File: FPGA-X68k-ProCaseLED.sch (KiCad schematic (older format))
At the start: 47 parts, among them J1 Conn_01x05_Male, SW1 SW_DIP_x04, U1 TLC59116IPWR

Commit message: First version
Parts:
- added TP25: RESET, TestPoint:TestPoint_THTPad_D1.5mm_Drill0.7mm, symbol Connector:TestPoint
- added TP26: SCL, TestPoint:TestPoint_THTPad_D1.5mm_Drill0.7mm, symbol Connector:TestPoint
- added TP27: SDA, TestPoint:TestPoint_THTPad_D1.5mm_Drill0.7mm, symbol Connector:TestPoint
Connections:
- net RESET: now also TP25.1
- net SCL: now also TP26.1
- net SDA: now also TP27.1
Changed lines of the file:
@@
 Connection ~ 2950 3850
 Wire Wire Line
-	1250 3850 2950 3850
+	1250 3850 2750 3850
 Connection ~ 2650 3750
 Wire Wire Line
 	2650 3750 3350 3750
 Wire Wire Line
-	1250 3750 2650 3750
+	1250 3750 2450 3750
 $Comp
 L power:+3.3V #PWR06
@@
 Connection ~ 2350 3650
 Wire Wire Line
-	2350 3650 1250 3650
+	2350 3650 2150 3650
 Text Label 1600 3650 0    50   ~ 0
 RESET
@@
 Wire Wire Line
 	4400 1700 4200 1700
+Connection ~ 4200 1700
+Wire Wire Line
+	4200 1700 4200 2050
+$Comp
+L Connector:TestPoint TP25
+U 1 1 5F30828E
+P 2150 3600
+F 0 "TP25" H 2208 3718 50  0000 L CNN
+F 1 "RESET" H 2208 3627 50  0000 L CNN
+F 2 "TestPoint:TestPoint_THTPad_D1.5mm_Drill0.7mm" H 2350 3600 50  0001 C CNN
+F 3 "~" H 2350 3600 50  0001 C CNN
+	1    2150 3600
+	1    0    0    -1
+$EndComp
+$Comp
+L Connector:TestPoint TP26
+U 1 1 5F308F76
+P 2450 3600
+F 0 "TP26" H 2508 3718 50  0000 L CNN
+F 1 "SCL" H 2508 3627 50  0000 L CNN
+F 2 "TestPoint:TestPoint_THTPad_D1.5mm_Drill0.7mm" H 2650 3600 50  0001 C CNN
+F 3 "~" H 2650 3600 50  0001 C CNN
+	1    2450 3600
+	1    0    0    -1
+$EndComp
+$Comp
+L Connector:TestPoint TP27
+U 1 1 5F3091EF
+P 2750 3600
+F 0 "TP27" H 2808 3718 50  0000 L CNN
+F 1 "SDA" H 2808 3627 50  0000 L CNN
+F 2 "TestPoint:TestPoint_THTPad_D1.5mm_Drill0.7mm" H 2950 3600 50  0001 C CNN
+F 3 "~" H 2950 3600 50  0001 C CNN
+	1    2750 3600
+	1    0    0    -1
+$EndComp
+Wire Wire Line
+	2150 3600 2150 3650
+Connection ~ 2150 3650
+Wire Wire Line
+	2150 3650 1250 3650
+Wire Wire Line
+	2450 3600 2450 3750
+Connection ~ 2450 3750
+Wire Wire Line
+	2450 3750 2650 3750
+Wire Wire Line
+	2750 3600 2750 3850
 Wire Bus Line
 	8150 700  8150 6400
@@
 Wire Bus Line
 	5350 2300 5350 6400
-Connection ~ 4200 1700
-Wire Wire Line
-	4200 1700 4200 2050
+Connection ~ 2750 3850
+Wire Wire Line
+	2750 3850 2950 3850
 $EndSCHEMATC

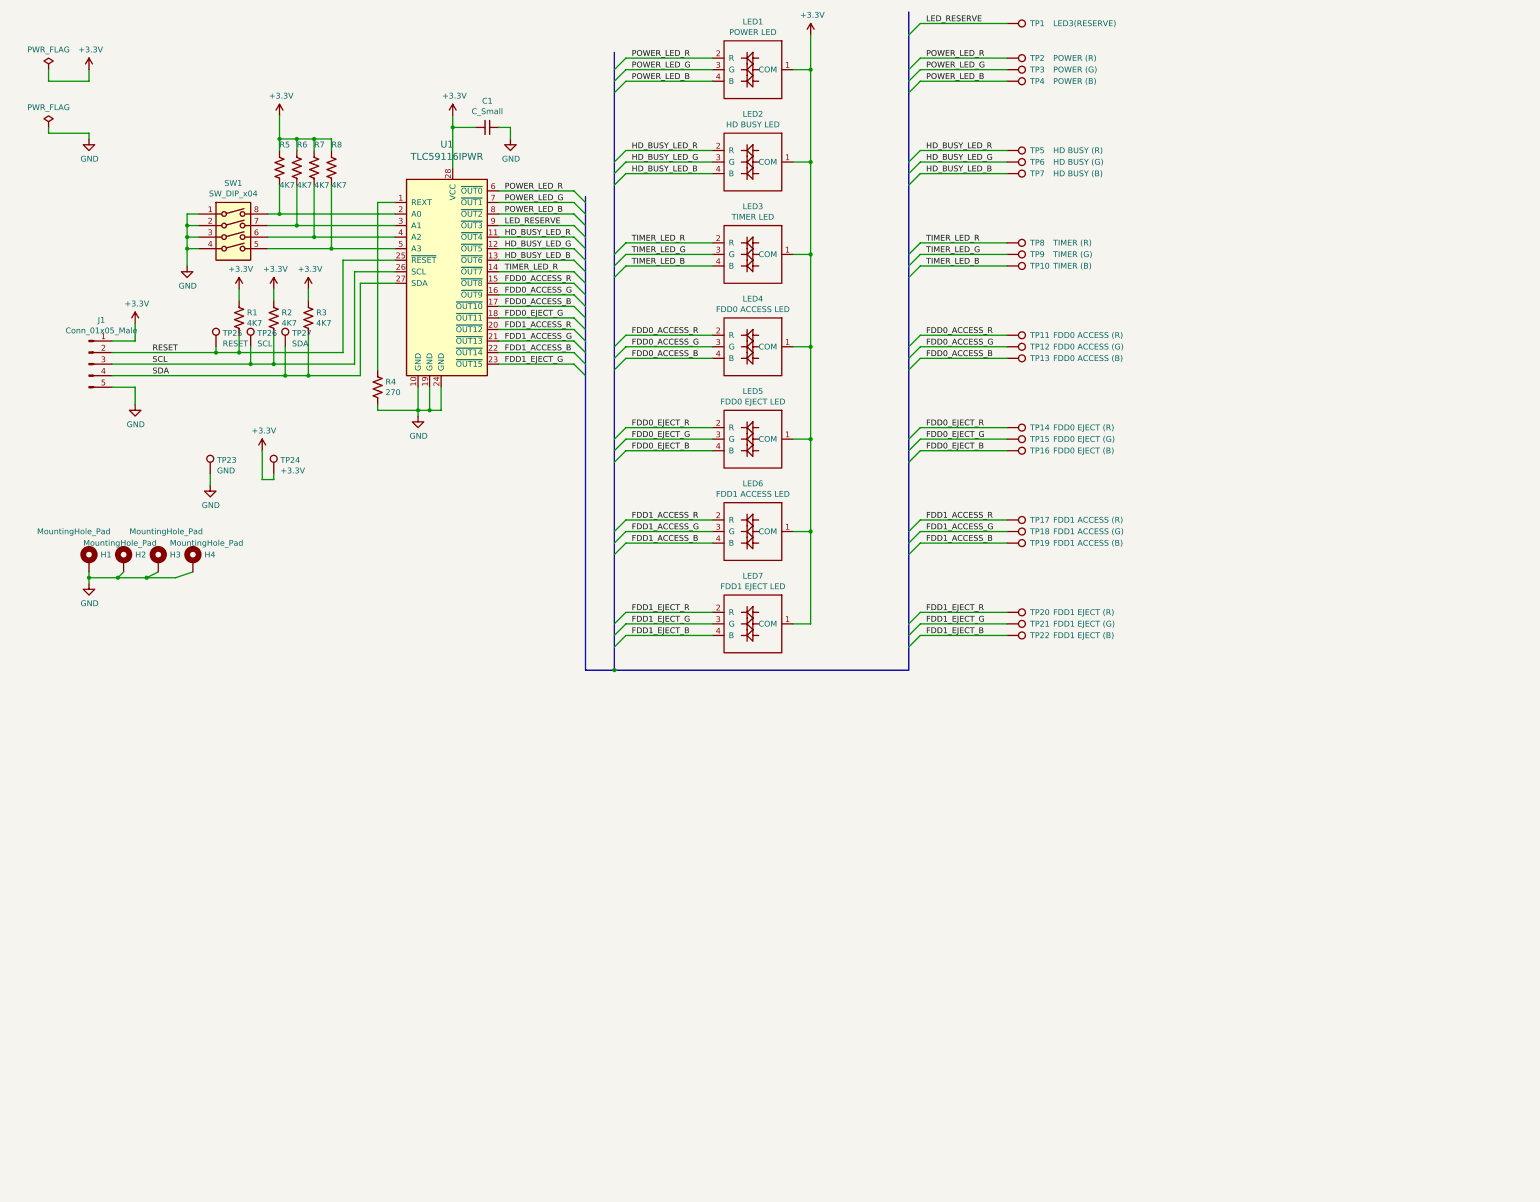
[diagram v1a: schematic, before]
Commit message: Add miniature FDD sensor circuit.
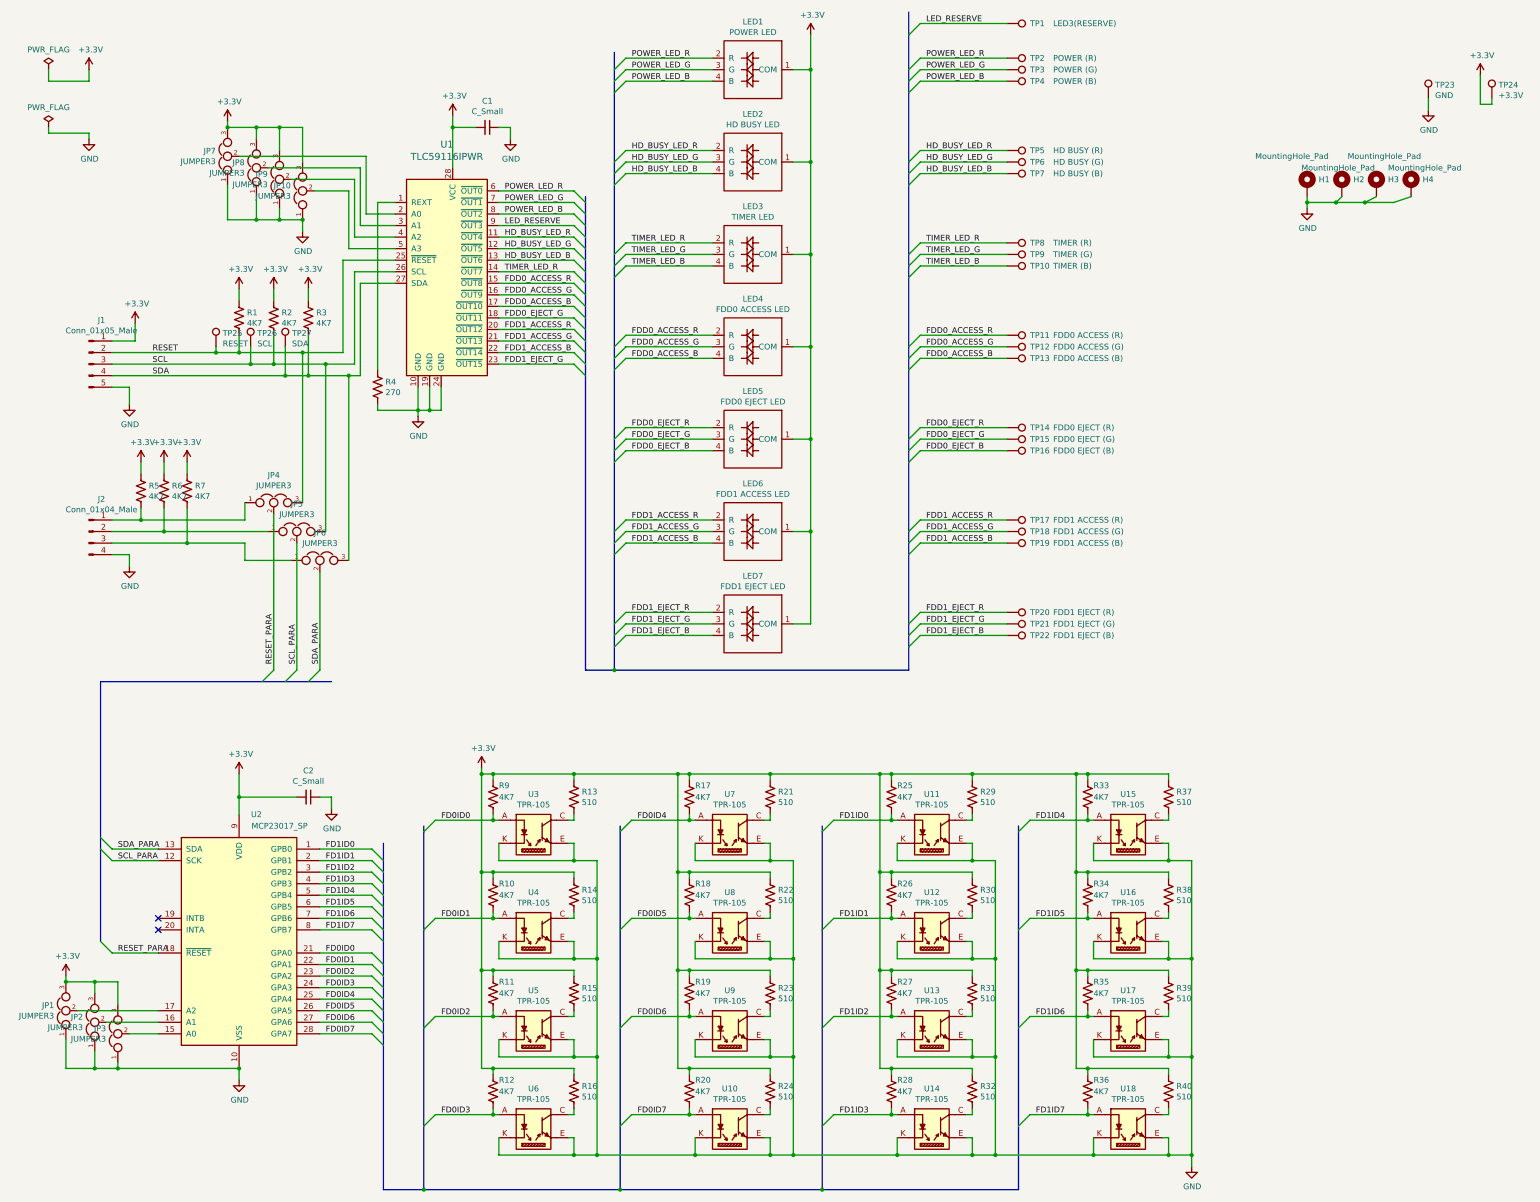
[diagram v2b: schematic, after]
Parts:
- removed R8: 4K7, Resistor_SMD:R_0603_1608Metric_Pad1.05x0.95mm_HandSolder, symbol Device:R_US
- removed SW1: SW_DIP_x04, Button_Switch_SMD:SW_DIP_SPSTx04_Slide_Copal_CHS-04B_W7.62mm_P1.27mm, symbol Switch:SW_DIP_x04
- added C2: C_Small, Capacitor_SMD:C_0603_1608Metric_Pad1.05x0.95mm_HandSolder, symbol Device:C_Small
- added J2: Conn_01x04_Male, Connector_JST:JST_EH_S4B-EH_1x04_P2.50mm_Horizontal, symbol Connector:Conn_01x04_Male
- added JP1, JP10, JP2, JP3, JP4, JP5, JP6, JP7, JP8, JP9: JUMPER3, Jumper:SolderJumper-3_P1.3mm_Open_RoundedPad1.0x1.5mm_NumberLabels, symbol device:JUMPER3
- added R10, R11, R12, R17, R18, R19, R20, R25, R26, R27, R28, R33, R34, R35, R36, R9: 4K7, Resistor_SMD:R_0603_1608Metric_Pad1.05x0.95mm_HandSolder, symbol Device:R_US
- added R13, R14, R15, R16, R21, R22, R23, R24, R29, R30, R31, R32, R37, R38, R39, R40: 510, Resistor_SMD:R_0603_1608Metric_Pad1.05x0.95mm_HandSolder, symbol Device:R_US
- added U10, U11, U12, U13, U14, U15, U16, U17, U18, U3, U4, U5, U6, U7, U8, U9: TPR-105, local:TPR-105, symbol local:TPR-105
- added U2: MCP23017_SP, Package_DIP:DIP-28_W7.62mm, symbol Interface_Expansion:MCP23017_SP
- TP1, TP10, TP11, TP12, TP13, TP14, TP15, TP16, TP17, TP18, TP19, TP2, TP20, TP21, TP22, TP3, TP4, TP5, TP6, TP7, TP8, TP9: footprint TestPoint:TestPoint_THTPad_D1.5mm_Drill0.7mm -> TestPoint:TestPoint_Pad_1.0x1.0mm
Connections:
- net +3V3: now also C2.2, JP1.3, JP10.3, JP2.3, JP3.3, JP7.3, JP8.3, JP9.3, R10.2, R11.2, R12.2, R13.2, R14.2, R15.2, R16.2, R17.2, R18.2, R19.2, R20.2, R21.2, R22.2, R23.2, R24.2, R25.2, R26.2, R27.2, R28.2, R29.2, R30.2, R31.2, R32.2, R33.2, R34.2, R35.2, R36.2, R37.2, R38.2, R39.2, R40.2, R9.2, U2.9 (VDD)
- net GND: now also C2.1, J2.4 (Pin_4), JP1.1, JP10.1, JP2.1, JP3.1, JP7.1, JP8.1, JP9.1, U10.E, U10.K, U11.E, U11.K, U12.E, U12.K, U13.E, U13.K, U14.E, U14.K, U15.E, U15.K, U16.E, U16.K, U17.E, U17.K, U18.E, U18.K, U2.10 (VSS), U3.E, U3.K, U4.E, U4.K, U5.E, U5.K, U6.E, U6.K, U7.E, U7.K, U8.E, U8.K, U9.E, U9.K
- net RESET: now also JP4.3
- net SCL: now also JP5.3
- net SDA: now also JP6.3
- net at U1.2 (A0): now also JP7.2; no longer R5.1
- net at U1.3 (A1): now also JP8.2; no longer R6.1
- net at U1.4 (A2): now also JP9.2; no longer R7.1
- net at U1.5 (A3): now also JP10.2
- new net: JP3.2, U2.15 (A0)
- new net: JP2.2, U2.16 (A1)
- new net: JP1.2, U2.17 (A2)
- new net: R13.1, U3.C
- new net: R14.1, U4.C
- new net: R15.1, U5.C
- new net: R16.1, U6.C
- new net: R21.1, U7.C
- new net: R22.1, U8.C
- new net: R23.1, U9.C
- new net: R24.1, U10.C
- new net: R29.1, U11.C
- new net: R30.1, U12.C
- new net: R31.1, U13.C
- new net: R32.1, U14.C
- new net: R37.1, U15.C
- new net: R38.1, U16.C
- new net: R39.1, U17.C
- new net: R40.1, U18.C
- new net: J2.2 (Pin_2), JP5.1, R6.1
- new net: J2.3 (Pin_3), JP6.1, R7.1
- new net: J2.1 (Pin_1), JP4.1, R5.1
- new net FD0ID0: R9.1, U2.21 (GPA0), U3.A
- new net FD0ID1: R10.1, U2.22 (GPA1), U4.A
- new net FD0ID2: R11.1, U2.23 (GPA2), U5.A
- new net FD0ID3: R12.1, U2.24 (GPA3), U6.A
- new net FD0ID4: R17.1, U2.25 (GPA4), U7.A
- new net FD0ID5: R18.1, U2.26 (GPA5), U8.A
- new net FD0ID6: R19.1, U2.27 (GPA6), U9.A
- new net FD0ID7: R20.1, U10.A, U2.28 (GPA7)
- new net FD1ID0: R25.1, U11.A, U2.1 (GPB0)
- new net FD1ID1: R26.1, U12.A, U2.2 (GPB1)
- new net FD1ID2: R27.1, U13.A, U2.3 (GPB2)
- new net FD1ID3: R28.1, U14.A, U2.4 (GPB3)
- new net FD1ID4: R33.1, U15.A, U2.5 (GPB4)
- new net FD1ID5: R34.1, U16.A, U2.6 (GPB5)
- new net FD1ID6: R35.1, U17.A, U2.7 (GPB6)
- new net FD1ID7: R36.1, U18.A, U2.8 (GPB7)
- new net RESET_PARA: JP4.2, U2.18 (~RESET~)
- new net SCL_PARA: JP5.2, U2.12 (SCK)
- new net SDA_PARA: JP6.2, U2.13 (SDA)
- no-connect marks 0 -> 2
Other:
- moved on the sheet: H1, H2, H3, H4, TP23, TP24
